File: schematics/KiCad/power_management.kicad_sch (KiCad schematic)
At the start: 52 parts, among them J3 USB_C, Q1 DMG6601LVT-7, Q2 DMG6601LVT-7, Q3 DMG9926UDM, SW4 TL1105SF160R, U4 AP2112K-3.3, U5 MP2615AGQ-Z, U6 BQ29700DSER

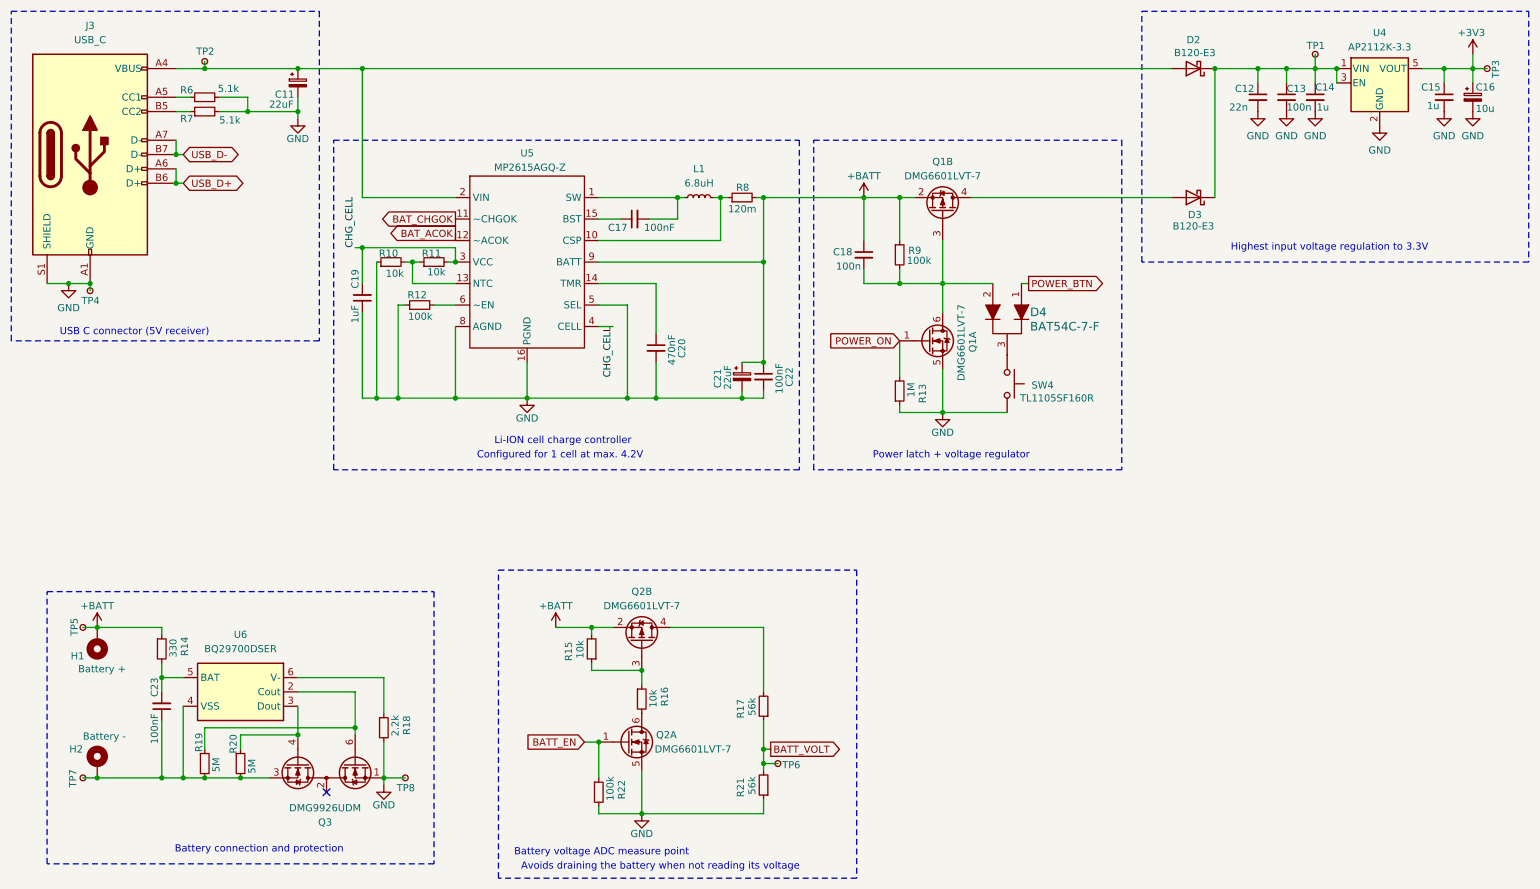
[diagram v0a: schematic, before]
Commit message: assign capacitors footprints
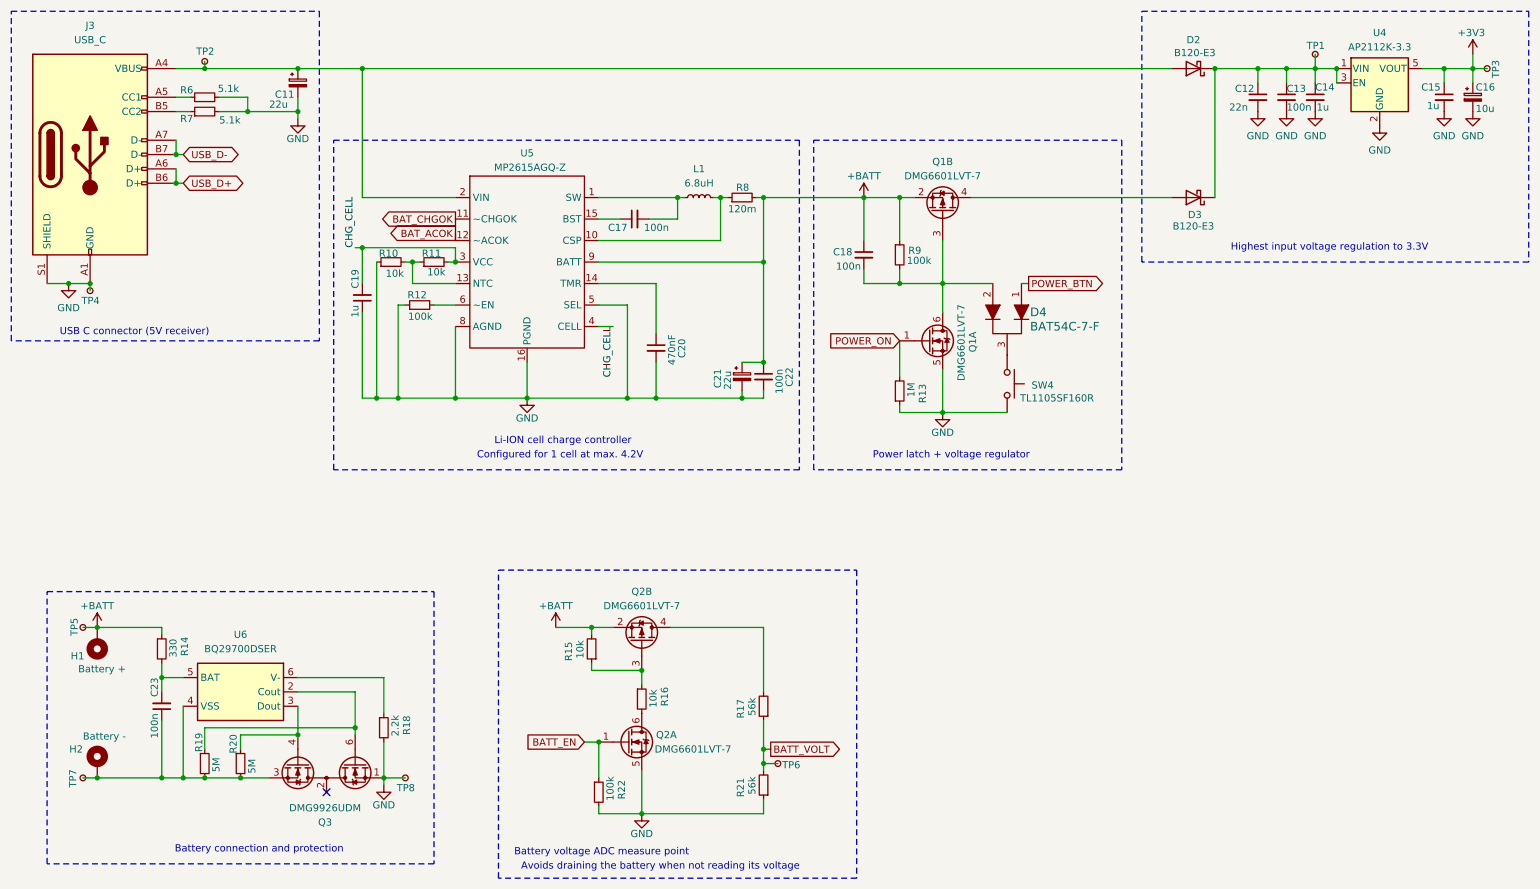
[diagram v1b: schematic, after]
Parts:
- C11, C21: value 22uF -> 22u; footprint (none) -> Capacitor_SMD:C_0603_1608Metric
- C13, C14, C15, C18: footprint Capacitor_SMD:C_0201_0603Metric -> Capacitor_SMD:C_0402_1005Metric
- C16: footprint (none) -> Capacitor_SMD:C_0402_1005Metric
- C17, C22, C23: value 100nF -> 100n; footprint Capacitor_SMD:C_0201_0603Metric -> Capacitor_SMD:C_0402_1005Metric
- C19: value 1uF -> 1u; footprint Capacitor_SMD:C_0201_0603Metric -> Capacitor_SMD:C_0402_1005Metric
- D4: footprint digikey-footprints:SOT-23-3 -> (none)
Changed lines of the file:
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@@
 	(title_block
 		(title "Leany power management")
-		(date "2024-09-06")
+		(date "2024-10-07")
 		(comment 1 "MIT License")
 		(comment 2 "Copyright (c) 2023 Gilles Henrard")
@@
 			)
 		)
-		(property "Value" "22uF"
+		(property "Value" "22u"
 			(at 140.97 87.376 90)
 			(effects
@@
 			)
 		)
-		(property "Footprint" ""
+		(property "Footprint" "Capacitor_SMD:C_0603_1608Metric"
 			(at 143.51 85.09 0)
 			(effects
@@
 			)
 		)
-		(property "Value" "100nF"
+		(property "Value" "100n"
 			(at 150.114 88.138 90)
 			(effects
@@
 			)
 		)
-		(property "Footprint" "Capacitor_SMD:C_0201_0603Metric"
+		(property "Footprint" "Capacitor_SMD:C_0402_1005Metric"
 			(at 147.32 85.09 0)
 			(effects
@@
 			)
 		)
-		(property "Footprint" "Capacitor_SMD:C_0201_0603Metric"
+		(property "Footprint" "Capacitor_SMD:C_0402_1005Metric"
 			(at 240.03 35.56 0)
 			(effects
@@
 			)
 		)
-		(property "Footprint" ""
+		(property "Footprint" "Capacitor_SMD:C_0402_1005Metric"
 			(at 273.05 35.56 0)
 			(effects
@@
 			)
 		)
-		(property "Value" "22uF"
+		(property "Value" "22u"
 			(at 59.69 36.83 0)
 			(effects
@@
 			)
 		)
-		(property "Footprint" ""
+		(property "Footprint" "Capacitor_SMD:C_0603_1608Metric"
 			(at 64.77 33.02 0)
 			(effects
@@
 			)
 		)
-		(property "Value" "1uF"
+		(property "Value" "1u"
 			(at 74.93 72.39 90)
 			(effects
@@
 			)
 		)
-		(property "Footprint" "Capacitor_SMD:C_0201_0603Metric"
+		(property "Footprint" "Capacitor_SMD:C_0402_1005Metric"
 			(at 76.2 71.12 0)
 			(effects
@@
 			)
 		)
-		(property "Footprint" "Capacitor_SMD:C_0201_0603Metric"
+		(property "Footprint" "Capacitor_SMD:C_0402_1005Metric"
 			(at 165.1 63.5 0)
 			(effects
@@
 			)
 		)
-		(property "Footprint" "digikey-footprints:SOT-23-3"
+		(property "Footprint" ""
 			(at 195.58 78.74 0)
 			(effects
@@
 			)
 		)
-		(property "Value" "100nF"
+		(property "Value" "100n"
 			(at 39.37 144.78 90)
 			(effects
@@
 			)
 		)
-		(property "Footprint" "Capacitor_SMD:C_0201_0603Metric"
+		(property "Footprint" "Capacitor_SMD:C_0402_1005Metric"
 			(at 40.64 143.51 0)
 			(effects
@@
 			)
 		)
-		(property "Footprint" "Capacitor_SMD:C_0201_0603Metric"
+		(property "Footprint" "Capacitor_SMD:C_0402_1005Metric"
 			(at 245.11 35.56 0)
 			(effects
@@
 			)
 		)
-		(property "Footprint" "Capacitor_SMD:C_0201_0603Metric"
+		(property "Footprint" "Capacitor_SMD:C_0402_1005Metric"
 			(at 267.97 35.56 0)
 			(effects
@@
 			)
 		)
-		(property "Value" "100nF"
-			(at 131.572 58.674 90)
+		(property "Value" "100n"
+			(at 130.556 58.674 90)
 			(effects
 				(font
@@
 			)
 		)
-		(property "Footprint" "Capacitor_SMD:C_0201_0603Metric"
+		(property "Footprint" "Capacitor_SMD:C_0402_1005Metric"
 			(at 124.46 57.15 0)
 			(effects

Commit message: fix misclicks
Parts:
- C12: footprint Capacitor_SMD:C_0201_0603Metric -> Capacitor_SMD:C_0402_1005Metric
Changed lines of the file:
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@@
 			)
 		)
-		(property "Footprint" "Capacitor_SMD:C_0201_0603Metric"
+		(property "Footprint" "Capacitor_SMD:C_0402_1005Metric"
 			(at 234.95 35.56 0)
 			(effects

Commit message: assign power latch diodes footprints
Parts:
- D4: footprint (none) -> Package_TO_SOT_SMD:SOT-23
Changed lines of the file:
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@@
 			)
 		)
-		(property "Footprint" ""
+		(property "Footprint" "Package_TO_SOT_SMD:SOT-23"
 			(at 195.58 78.74 0)
 			(effects
